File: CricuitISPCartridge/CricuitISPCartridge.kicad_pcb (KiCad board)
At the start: 2 copper layers, 27.9 x 26.7 mm, 3 parts, among them J1 Conn_02x10_Odd_Even, J2 Conn_01x03_Male, J3 AVR-ISP-6

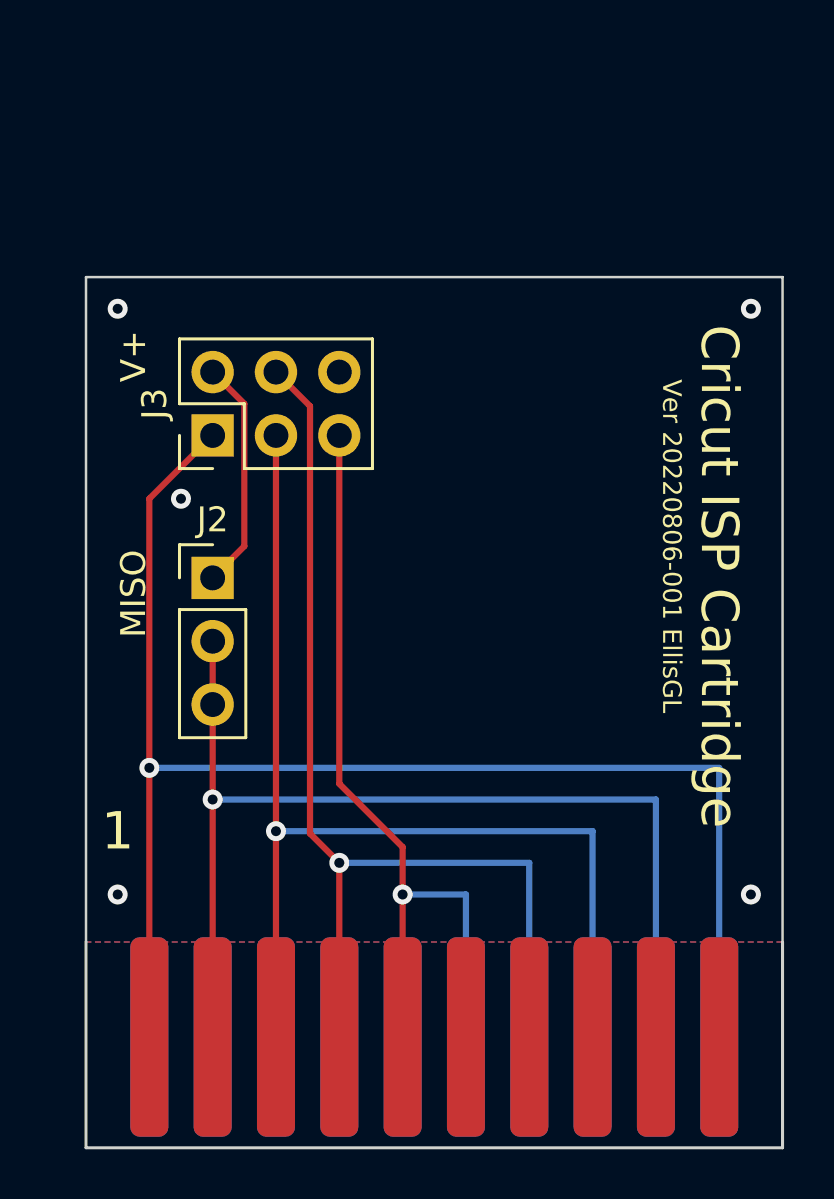
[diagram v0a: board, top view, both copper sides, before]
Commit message: Roudning the traces. Thank you new KiCad!
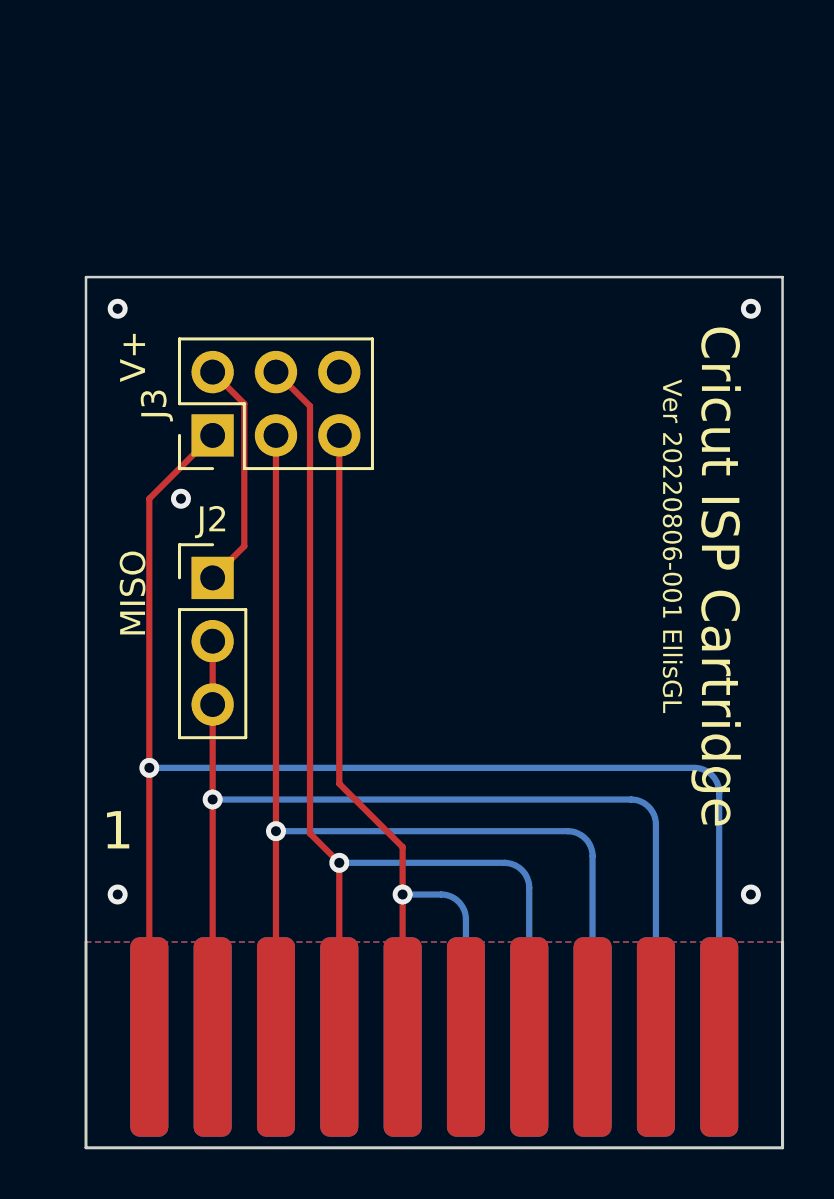
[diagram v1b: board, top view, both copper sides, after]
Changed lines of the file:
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@@
 	)
 	(segment
-		(start 82.55 111.125)
+		(start 81.55 111.125)
 		(end 59.69 111.125)
 		(width 0.25)
@@
 	)
 	(segment
-		(start 82.55 111.125)
+		(start 82.55 112.125)
 		(end 82.55 121.92)
+		(width 0.25)
+		(layer "B.Cu")
+		(net 1)
+	)
+	(arc
+		(start 81.55 111.125)
+		(mid 82.257106 111.417893)
+		(end 82.55 112.125)
 		(width 0.25)
 		(layer "B.Cu")
@@
 	)
 	(segment
-		(start 80.01 112.395)
+		(start 80.01 113.395)
+		(end 80.01 121.92)
+		(width 0.25)
+		(layer "B.Cu")
+		(net 3)
+	)
+	(segment
+		(start 79.01 112.395)
 		(end 62.23 112.395)
 		(width 0.25)
@@
 		(net 3)
 	)
-	(segment
-		(start 80.01 112.395)
-		(end 80.01 121.92)
+	(arc
+		(start 79.01 112.395)
+		(mid 79.717106 112.687893)
+		(end 80.01 113.395)
 		(width 0.25)
 		(layer "B.Cu")
@@
 	)
 	(segment
-		(start 64.77 113.665)
-		(end 77.47 113.665)
-		(width 0.25)
-		(layer "B.Cu")
-		(net 5)
-	)
-	(segment
-		(start 77.47 113.665)
+		(start 76.47 113.665)
+		(end 64.77 113.665)
+		(width 0.25)
+		(layer "B.Cu")
+		(net 5)
+	)
+	(segment
+		(start 77.47 114.665)
 		(end 77.47 121.92)
+		(width 0.25)
+		(layer "B.Cu")
+		(net 5)
+	)
+	(arc
+		(start 76.47 113.665)
+		(mid 77.177106 113.957893)
+		(end 77.47 114.665)
 		(width 0.25)
 		(layer "B.Cu")
@@
 	)
 	(segment
-		(start 74.93 114.935)
+		(start 73.93 114.935)
 		(end 67.31 114.935)
 		(width 0.25)
@@
 	)
 	(segment
-		(start 74.93 114.935)
+		(start 74.93 115.935)
 		(end 74.93 121.92)
+		(width 0.25)
+		(layer "B.Cu")
+		(net 7)
+	)
+	(arc
+		(start 73.93 114.935)
+		(mid 74.637106 115.227893)
+		(end 74.93 115.935)
 		(width 0.25)
 		(layer "B.Cu")
@@
 	)
 	(segment
-		(start 72.39 116.205)
+		(start 71.39 116.205)
+		(end 69.85 116.205)
+		(width 0.25)
+		(layer "B.Cu")
+		(net 9)
+	)
+	(segment
+		(start 72.39 117.205)
 		(end 72.39 121.92)
 		(width 0.25)
@@
 		(net 9)
 	)
-	(segment
-		(start 72.39 116.205)
-		(end 69.85 116.205)
-		(width 0.25)
-		(layer "B.Cu")
+	(arc
+		(start 72.39 117.205)
+		(mid 72.097106 116.497893)
+		(end 71.39 116.205)
+		(width 0.25)
+		(layer "B.Cu")

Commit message: Updated the ISP addapter card PCB. Now with 100% more visable labeling
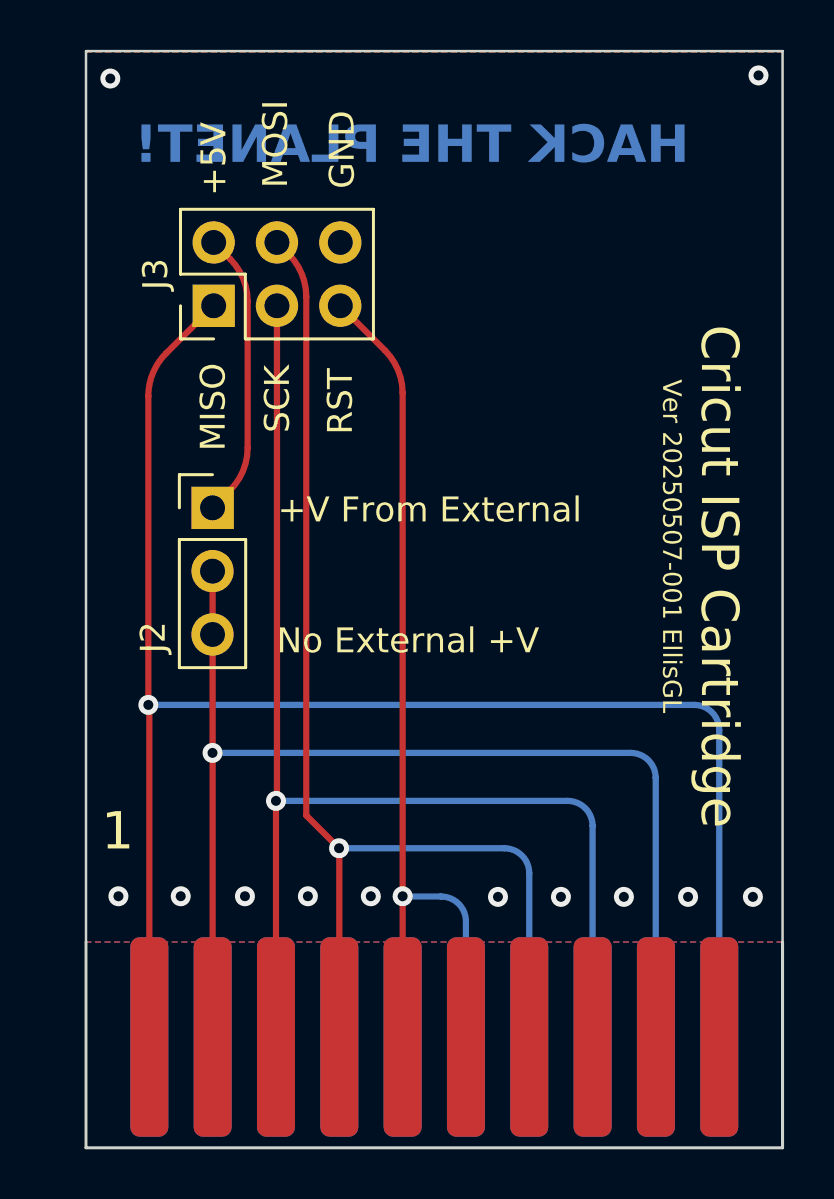
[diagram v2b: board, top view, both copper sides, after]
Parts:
- moved J3 5.20 mm to (62.3, 92.6)
- moved J2 2.81 mm to (62.2, 100.7)
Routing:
- net MISO: track 58.4 -> 66.1 mm
- net SCK: track 44.6 -> 51.0 mm
- net MOSI: track 41.9 -> 47.5 mm
- net RST: track 33.0 -> 38.0 mm
- net VCC: track 42.7 -> 47.4 mm
- net +5V: track 9.31 -> 11.6 mm
- net GND: vias 5 -> 12
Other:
- board size 27.9 x 26.7 mm -> 27.9 x 35.7 mm
- board text added: "+5V"
- board text added: "+V From External"
- board text added: "GND"
- board text added: "HACK THE PLANET!"
- board text added: "MOSI"
- board text added: "No External +V"
- board text added: "RST"
- board text added: "SCK"
- board text added: "Ver 20250507-001 EllisGL"
- board text removed: "V+"
- board text removed: "Ver 20220806-001 EllisGL"

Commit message: Might as well break out all the ports for the cartridge slot.
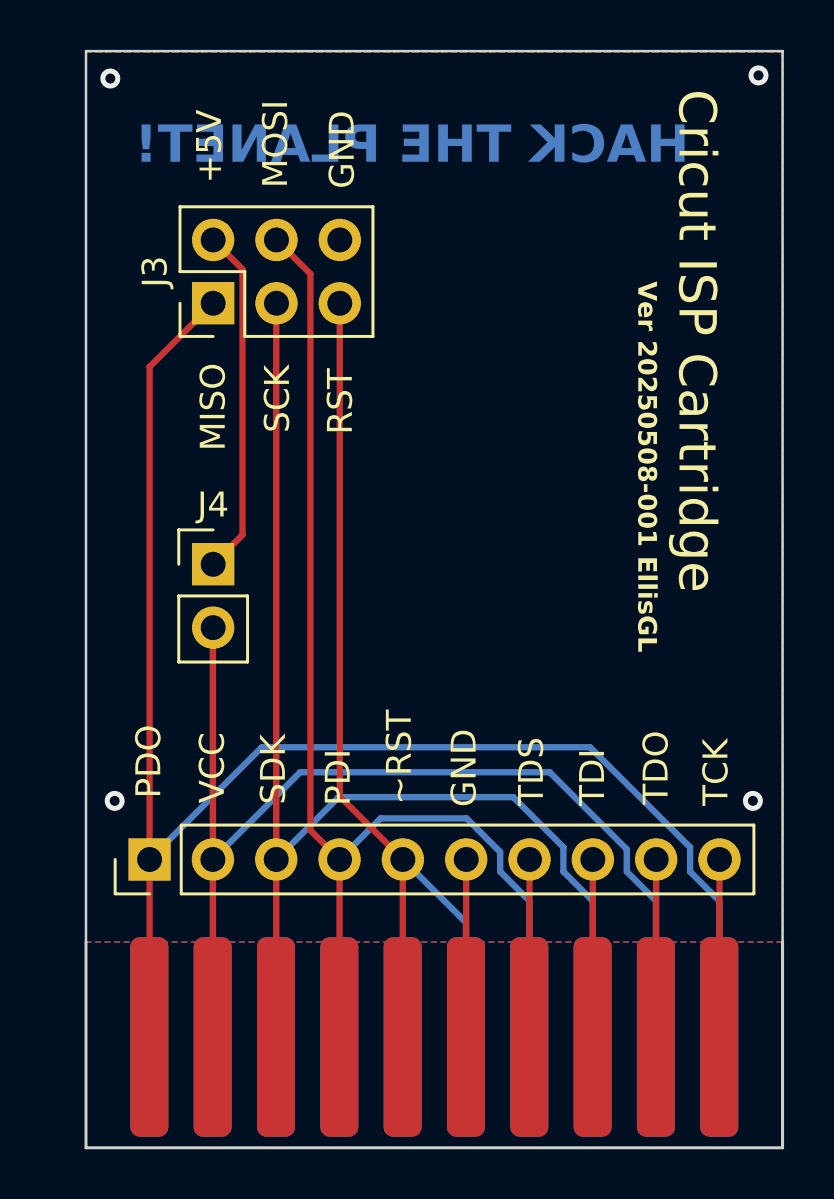
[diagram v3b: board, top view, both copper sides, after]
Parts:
- added J4: Conn_01x02_Pin, Connector_PinHeader_2.54mm:PinHeader_1x02_P2.54mm_Vertical, F.Cu at (62.2, 103.0)
- J2: value Conn_01x03_Male -> Conn_01x10_Pin; footprint Connector_PinHeader_2.54mm:PinHeader_1x03_P2.54mm_Vertical -> Connector_PinHeader_2.54mm:PinHeader_1x10_P2.54mm_Vertical
- moved J2 14.3 mm to (59.7, 114.8), turned to 90 degrees
- moved J3 0.10 mm to (62.2, 92.5)
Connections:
- J1 pad 1: MISO -> PDO/MISO
- J1 pad 12: RST -> ~{RST}
- J1 pad 13: unconnected-(J1-Pad13) -> TDS
- J1 pad 14: MOSI -> PDI/MOSI
- J1 pad 15: unconnected-(J1-Pad15) -> TDI
- J1 pad 17: unconnected-(J1-Pad17) -> TDO
- J1 pad 19: unconnected-(J1-Pad19) -> TCK
- J1 pad 2: unconnected-(J1-Pad2) -> TCK
- J1 pad 20: MISO -> PDO/MISO
- J1 pad 4: unconnected-(J1-Pad4) -> TDO
- J1 pad 6: unconnected-(J1-Pad6) -> TDI
- J1 pad 7: MOSI -> PDI/MOSI
- J1 pad 8: unconnected-(J1-Pad8) -> TDS
- J1 pad 9: RST -> ~{RST}
- J2 pad 1: +5V -> PDO/MISO
- J2 pad 3: VCC -> SCK
- J3 pad 1: MISO -> PDO/MISO
- J3 pad 4: MOSI -> PDI/MOSI
- J3 pad 5: RST -> ~{RST}
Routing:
- net MISO: track 66.1 -> 0.00 mm, vias 1 -> 0
- net PDO/MISO: track 0.00 -> 63.8 mm
- net PDI/MOSI: track 0.00 -> 48.6 mm
- net MOSI: track 47.5 -> 0.00 mm, vias 1 -> 0
- net ~{RST}: track 0.00 -> 38.7 mm
- net RST: track 38.0 -> 0.00 mm, vias 1 -> 0
- net TDI: track 0.00 -> 7.12 mm
- net TCK: track 0.00 -> 7.12 mm
- net GND: track 0.00 -> 7.12 mm, vias 12 -> 4
- net TDS: track 0.00 -> 7.12 mm
- net TDO: track 0.00 -> 7.12 mm
- net VCC: track 47.4 -> 43.8 mm, vias 1 -> 0
- net +5V: track 11.6 -> 14.0 mm
- net SCK: track 51.0 -> 50.9 mm, vias 1 -> 0
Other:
- board text added: "PDI"
- board text added: "PDO"
- board text added: "SDK"
- board text added: "TCK"
- board text added: "TDI"
- board text added: "TDO"
- board text added: "TDS"
- board text added: "VCC"
- board text added: "Ver 20250508-001 EllisGL"
- board text added: "~RST"
- board text removed: "+V From External"
- board text removed: "1"
- board text removed: "No External +V"
- board text removed: "Ver 20250507-001 EllisGL"
